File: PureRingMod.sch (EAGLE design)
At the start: 37 parts, among them IC1 TL074P, IC2 TL072P, X1 NC3FD-V

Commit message: Fixed output socket
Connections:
- net GND: no longer OUTPUT.NORM
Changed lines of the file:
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@@
 <wire x1="149.86" y1="60.96" x2="149.86" y2="58.42" width="0.1524" layer="91"/>
 <label x="149.86" y="55.88" size="1.778" layer="95"/>
-<pinref part="OUTPUT" gate="G$1" pin="NORM"/>
-<wire x1="152.4" y1="63.5" x2="149.86" y2="63.5" width="0.1524" layer="91"/>
-<wire x1="149.86" y1="63.5" x2="149.86" y2="60.96" width="0.1524" layer="91"/>
-<junction x="149.86" y="60.96"/>
 </segment>
 <segment>

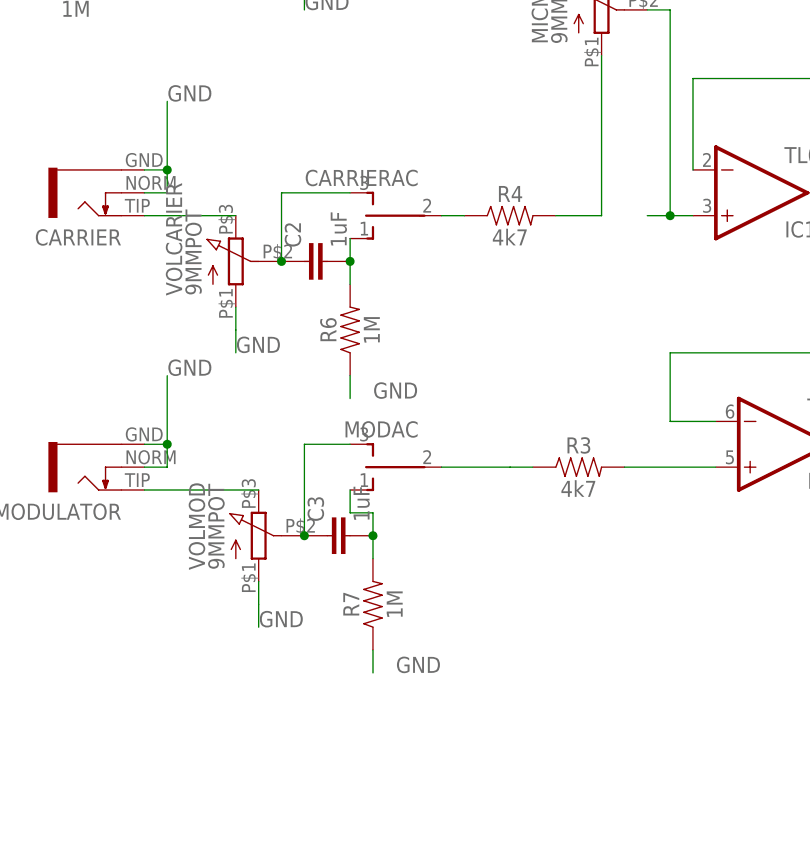
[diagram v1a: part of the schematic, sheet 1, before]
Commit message: removed ac/Dc switched input
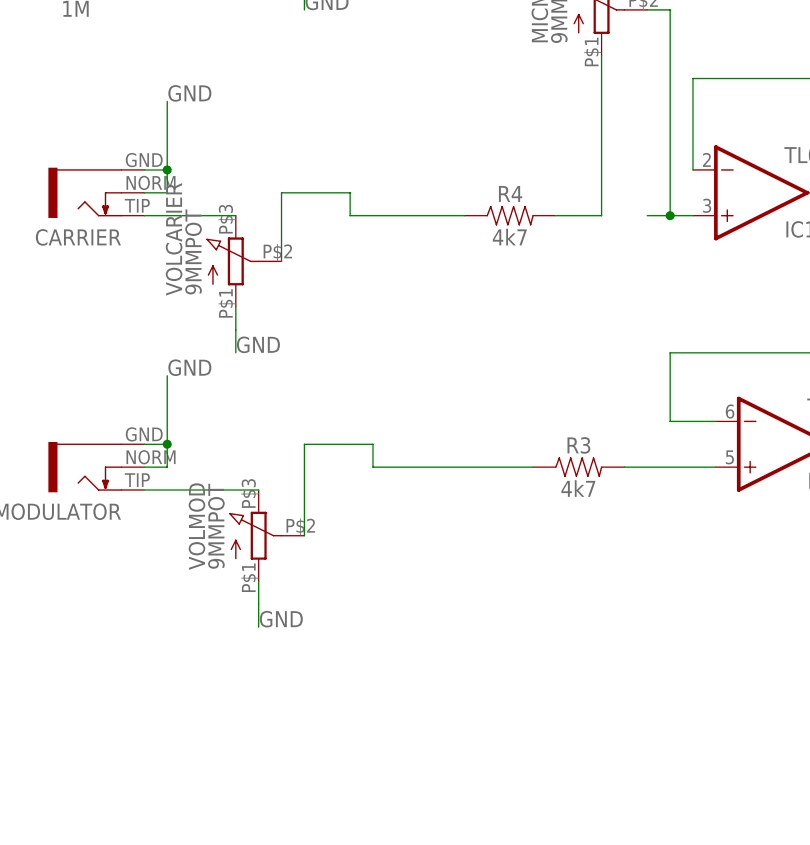
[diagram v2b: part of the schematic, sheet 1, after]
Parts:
- removed C2, C3: 1uF, SparkFun-Capacitors:0.1UF-KIT-EZ-50V-20%
- removed CARRIERAC, MODAC: TOGGLE_ON_OFF_ON, INSTRUO:TOGGLE_ON_OFF_ON
- removed R6, R7: 1M, SparkFun-Resistors:330OHM-HORIZ-1/10W-5%
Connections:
- removed net N$14: MODAC.P, R3.1
- removed net N$20: C2.2, CARRIERAC.O, R6.2
- removed net N$21: C3.2, MODAC.O, R7.2
- removed net N$8: CARRIERAC.P, R4.1
- net GND: no longer R6.1, R7.1
- net N$18: now also R4.1; no longer C2.1, CARRIERAC.S
- net N$19: now also R3.1; no longer C3.1, MODAC.S
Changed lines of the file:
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@@
 <part name="CARRIER" library="INSTRUO" deviceset="S_JACK" device="" value=""/>
 <part name="MODULATOR" library="INSTRUO" deviceset="S_JACK" device="" value=""/>
-<part name="CARRIERAC" library="INSTRUO" deviceset="TOGGLE_ON_OFF_ON" device="" value=""/>
-<part name="MODAC" library="INSTRUO" deviceset="TOGGLE_ON_OFF_ON" device="" value=""/>
 <part name="VOLCARIER" library="GMSN" deviceset="9MMPOT" device=""/>
 <part name="VOLMOD" library="GMSN" deviceset="9MMPOT" device=""/>
-<part name="C2" library="SparkFun-Capacitors" deviceset="0.1UF" device="-KIT-EZ-50V-20%" value="1uF"/>
-<part name="C3" library="SparkFun-Capacitors" deviceset="0.1UF" device="-KIT-EZ-50V-20%" value="1uF"/>
-<part name="R6" library="SparkFun-Resistors" deviceset="330OHM" device="-HORIZ-1/10W-5%" value="1M"/>
-<part name="R7" library="SparkFun-Resistors" deviceset="330OHM" device="-HORIZ-1/10W-5%" value="1M"/>
 <part name="X1" library="con-neutrik_ag" library_urn="urn:adsk.eagle:library:166" deviceset="NC3" device="FD-V" package3d_urn="urn:adsk.eagle:package:8819/1">
 <attribute name="RS-PART" value="448-244"/>
@@
 <attribute name="VALUE" x="-55.88" y="44.196" size="1.778" layer="96" rot="R180"/>
 </instance>
-<instance part="CARRIERAC" gate="G$1" x="-25.4" y="66.04" rot="R90">
-<attribute name="NAME" x="-22.86" y="71.12" size="1.778" layer="95" rot="R180"/>
-<attribute name="VALUE" x="-22.86" y="73.66" size="1.778" layer="96" rot="R180"/>
-</instance>
-<instance part="MODAC" gate="G$1" x="-25.4" y="38.1" rot="R90">
-<attribute name="NAME" x="-22.86" y="43.18" size="1.778" layer="95" rot="R180"/>
-<attribute name="VALUE" x="-22.86" y="45.72" size="1.778" layer="96" rot="R180"/>
-</instance>
 <instance part="VOLCARIER" gate="G$1" x="-43.18" y="60.96" rot="R90">
 <attribute name="NAME" x="-49.149" y="57.15" size="1.778" layer="95" rot="R90"/>
@@
 <attribute name="NAME" x="-46.609" y="26.67" size="1.778" layer="95" rot="R90"/>
 <attribute name="VALUE" x="-44.45" y="26.67" size="1.778" layer="96" rot="R90"/>
-</instance>
-<instance part="C2" gate="G$1" x="-33.02" y="60.96" rot="R90">
-<attribute name="NAME" x="-35.941" y="62.484" size="1.778" layer="95" font="vector" rot="R90"/>
-<attribute name="VALUE" x="-30.861" y="62.484" size="1.778" layer="96" font="vector" rot="R90"/>
-</instance>
-<instance part="C3" gate="G$1" x="-30.48" y="30.48" rot="R90">
-<attribute name="NAME" x="-33.401" y="32.004" size="1.778" layer="95" font="vector" rot="R90"/>
-<attribute name="VALUE" x="-28.321" y="32.004" size="1.778" layer="96" font="vector" rot="R90"/>
-</instance>
-<instance part="R6" gate="G$1" x="-30.48" y="53.34" rot="R90">
-<attribute name="NAME" x="-32.004" y="53.34" size="1.778" layer="95" font="vector" rot="R90" align="bottom-center"/>
-<attribute name="VALUE" x="-28.956" y="53.34" size="1.778" layer="96" font="vector" rot="R90" align="top-center"/>
-</instance>
-<instance part="R7" gate="G$1" x="-27.94" y="22.86" rot="R90">
-<attribute name="NAME" x="-29.464" y="22.86" size="1.778" layer="95" font="vector" rot="R90" align="bottom-center"/>
-<attribute name="VALUE" x="-26.416" y="22.86" size="1.778" layer="96" font="vector" rot="R90" align="top-center"/>
 </instance>
 <instance part="X1" gate="G$1" x="-116.84" y="104.14" rot="R180">
@@
 </segment>
 <segment>
-<pinref part="R6" gate="G$1" pin="1"/>
-<wire x1="-30.48" y1="48.26" x2="-30.48" y2="45.72" width="0.1524" layer="91"/>
-<label x="-27.94" y="45.72" size="1.778" layer="95"/>
-</segment>
-<segment>
-<pinref part="R7" gate="G$1" pin="1"/>
-<wire x1="-27.94" y1="17.78" x2="-27.94" y2="15.24" width="0.1524" layer="91"/>
-<label x="-25.4" y="15.24" size="1.778" layer="95"/>
-</segment>
-<segment>
 <pinref part="X1" gate="G$1" pin="G"/>
 <wire x1="-109.22" y1="109.22" x2="-104.14" y2="109.22" width="0.1524" layer="91"/>
@@
 </segment>
 </net>
-<net name="N$14" class="0">
-<segment>
-<pinref part="R3" gate="G$1" pin="1"/>
-<wire x1="-10.16" y1="38.1" x2="-12.7" y2="38.1" width="0.1524" layer="91"/>
-<pinref part="MODAC" gate="G$1" pin="P"/>
-<wire x1="-20.32" y1="38.1" x2="-12.7" y2="38.1" width="0.1524" layer="91"/>
-</segment>
-</net>
 <net name="N$15" class="0">
 <segment>
@@
 <segment>
 <pinref part="VOLCARIER" gate="G$1" pin="2"/>
-<pinref part="C2" gate="G$1" pin="1"/>
 <wire x1="-38.1" y1="60.96" x2="-38.1" y2="68.58" width="0.1524" layer="91"/>
-<junction x="-38.1" y="60.96"/>
-<pinref part="CARRIERAC" gate="G$1" pin="S"/>
 <wire x1="-38.1" y1="68.58" x2="-30.48" y2="68.58" width="0.1524" layer="91"/>
+<wire x1="-30.48" y1="68.58" x2="-30.48" y2="66.04" width="0.1524" layer="91"/>
+<pinref part="R4" gate="G$1" pin="1"/>
+<wire x1="-30.48" y1="66.04" x2="-17.78" y2="66.04" width="0.1524" layer="91"/>
 </segment>
 </net>
@@
 <segment>
 <pinref part="VOLMOD" gate="G$1" pin="2"/>
-<pinref part="C3" gate="G$1" pin="1"/>
 <wire x1="-35.56" y1="30.48" x2="-35.56" y2="40.64" width="0.1524" layer="91"/>
-<junction x="-35.56" y="30.48"/>
-<pinref part="MODAC" gate="G$1" pin="S"/>
-<wire x1="-30.48" y1="40.64" x2="-35.56" y2="40.64" width="0.1524" layer="91"/>
-</segment>
-</net>
-<net name="N$20" class="0">
-<segment>
-<pinref part="C2" gate="G$1" pin="2"/>
-<pinref part="CARRIERAC" gate="G$1" pin="O"/>
-<wire x1="-30.48" y1="60.96" x2="-30.48" y2="63.5" width="0.1524" layer="91"/>
-<pinref part="R6" gate="G$1" pin="2"/>
-<wire x1="-30.48" y1="60.96" x2="-30.48" y2="58.42" width="0.1524" layer="91"/>
-<junction x="-30.48" y="60.96"/>
-</segment>
-</net>
-<net name="N$21" class="0">
-<segment>
-<pinref part="C3" gate="G$1" pin="2"/>
-<wire x1="-27.94" y1="30.48" x2="-27.94" y2="33.02" width="0.1524" layer="91"/>
-<wire x1="-27.94" y1="33.02" x2="-30.48" y2="33.02" width="0.1524" layer="91"/>
-<pinref part="MODAC" gate="G$1" pin="O"/>
-<wire x1="-30.48" y1="33.02" x2="-30.48" y2="35.56" width="0.1524" layer="91"/>
-<pinref part="R7" gate="G$1" pin="2"/>
-<wire x1="-27.94" y1="30.48" x2="-27.94" y2="27.94" width="0.1524" layer="91"/>
-<junction x="-27.94" y="30.48"/>
+<wire x1="-27.94" y1="40.64" x2="-35.56" y2="40.64" width="0.1524" layer="91"/>
+<wire x1="-27.94" y1="40.64" x2="-27.94" y2="38.1" width="0.1524" layer="91"/>
+<pinref part="R3" gate="G$1" pin="1"/>
+<wire x1="-27.94" y1="38.1" x2="-10.16" y2="38.1" width="0.1524" layer="91"/>
 </segment>
 </net>
@@
 </segment>
 </net>
-<net name="N$8" class="0">
-<segment>
-<pinref part="CARRIERAC" gate="G$1" pin="P"/>
-<pinref part="R4" gate="G$1" pin="1"/>
-<wire x1="-20.32" y1="66.04" x2="-17.78" y2="66.04" width="0.1524" layer="91"/>
-</segment>
-</net>
